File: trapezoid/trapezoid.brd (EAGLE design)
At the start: 59.7 x 28.6 mm, 33 parts, among them U1 MMA8452Q, U4 MCP73831, Y1 CRYSTAL.ABS25

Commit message: silk
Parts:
- C6: value 0.1uF -> 1.0uF
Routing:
- net N$9: track 5.24 -> 5.87 mm
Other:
- board text added: "0.1uF"
- board text added: "1.0uF"
- board text added: "10"
- board text added: "10k"
- board text added: "11"
- board text added: "12"
- board text added: "13"
- board text added: "2"
- board text added: "2k"
- board text added: "330"
- board text added: "4.7uF"
- board text added: "47k"
- board text added: "ABS25"
- board text added: "CR1225"
- board text added: "DS1339"
- board text added: "FXAS21002"
- board text added: "GND"
- board text added: "MCP73831"
- board text added: "MMA8452Q"
- board text added: "Micron uSD"
- board text added: "RAW"
- board text added: "Sharkduino V2"
- board text added: "VCC"
- board text added: "VIMS"
- board text added: "W&M Physics"
- board text added: "W&M Physics VIMS"
- board text added: "William Laney"
- board text added: "William Laney 2016"
- board text added: "X"
- board text added: "Y"
- board text added: "Z"
- board text added: "uUSB"
- board text added: "welaney@email.wm.edu"
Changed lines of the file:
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@@
 <wire x1="22.225" y1="1.27" x2="22.225" y2="19.05" width="0.3048" layer="21"/>
 <circle x="36.4236" y="11.811" radius="0.289603125" width="0.254" layer="21"/>
+<wire x1="23.876" y1="20.193" x2="24.892" y2="20.193" width="0.254" layer="21"/>
+<wire x1="23.876" y1="20.193" x2="24.257" y2="19.812" width="0.254" layer="21"/>
+<wire x1="23.876" y1="20.193" x2="24.257" y2="20.574" width="0.254" layer="21"/>
+<wire x1="26.289" y1="20.701" x2="26.289" y2="19.685" width="0.254" layer="21"/>
+<wire x1="26.289" y1="20.701" x2="25.908" y2="20.32" width="0.254" layer="21"/>
+<wire x1="26.289" y1="20.701" x2="26.67" y2="20.32" width="0.254" layer="21"/>
+<circle x="22.733" y="20.193" radius="0.127" width="0.254" layer="21"/>
+<text x="25.781" y="21.717" size="1.016" layer="21" font="vector" ratio="15" rot="R270">X</text>
+<text x="24.003" y="21.717" size="1.016" layer="21" font="vector" ratio="15" rot="R270">Y</text>
+<text x="22.225" y="21.717" size="1.016" layer="21" font="vector" ratio="15" rot="R270">Z</text>
+<text x="8.509" y="15.24" size="1.016" layer="21" font="vector" ratio="15">Sharkduino V2</text>
+<text x="35.56" y="24.892" size="0.8128" layer="21" font="vector" ratio="15" rot="R90">0.1uF</text>
+<text x="37.592" y="21.844" size="0.8128" layer="21" font="vector" ratio="15" rot="R90">10k</text>
+<text x="41.402" y="21.844" size="0.8128" layer="21" font="vector" ratio="15" rot="R90">330</text>
+<text x="45.466" y="22.098" size="0.8128" layer="21" font="vector" ratio="15">4.7uF</text>
+<text x="51.054" y="26.924" size="0.8128" layer="21" font="vector" ratio="15">2k</text>
+<text x="50.546" y="19.558" size="0.8128" layer="21" font="vector" ratio="15" rot="R90">4.7uF</text>
+<text x="44.704" y="15.494" size="0.8128" layer="21" font="vector" ratio="15">0.1uF</text>
+<text x="50.8" y="10.0965" size="0.8128" layer="21" font="vector" ratio="15" rot="R90">0.1uF</text>
+<text x="30.2514" y="11.2014" size="0.8128" layer="21" font="vector" ratio="15" rot="R90">0.1uF</text>
+<text x="27.686" y="11.176" size="0.8128" layer="21" font="vector" ratio="15" rot="R90">1.0uF</text>
+<text x="32.1056" y="9.6774" size="0.8128" layer="21" font="vector" ratio="15">0.1uF</text>
+<text x="28.321" y="9.7028" size="0.8128" layer="21" font="vector" ratio="15">0.1uF</text>
+<text x="38.608" y="4.572" size="0.8128" layer="21" font="vector" ratio="15" rot="R90">10k</text>
+<text x="44.958" y="4.572" size="0.8128" layer="21" font="vector" ratio="15" rot="R90">10k</text>
+<text x="39.624" y="9.144" size="0.8128" layer="21" font="vector" ratio="15" rot="R90">10k</text>
+<text x="35.306" y="5.588" size="0.8128" layer="21" font="vector" ratio="15">47k</text>
+<text x="46.2915" y="10.0965" size="0.8128" layer="21" font="vector" ratio="15" rot="R90">4.7uF</text>
+<text x="22.352" y="27.178" size="0.8128" layer="21" font="vector" ratio="15">ABS25</text>
+<text x="29.972" y="25.146" size="0.8128" layer="21" font="vector" ratio="15">DS1339</text>
+<text x="33.528" y="15.24" size="0.8128" layer="21" font="vector" ratio="15">FXAS21002</text>
+<text x="41.275" y="8.8265" size="0.8128" layer="21" font="vector" ratio="15">MMA8452Q</text>
+<text x="40.4495" y="25.146" size="0.8128" layer="21" font="vector" ratio="15">MCP73831</text>
+<text x="9.652" y="2.286" size="0.8128" layer="21" font="vector" ratio="15">CR1225</text>
+<text x="59.436" y="11.049" size="0.8128" layer="21" font="vector" ratio="15" rot="R90">RAW</text>
+<text x="59.436" y="8.382" size="0.8128" layer="21" font="vector" ratio="15" rot="R90">GND</text>
+<text x="47.879" y="0.254" size="0.8128" layer="21" font="vector" ratio="15">GND</text>
+<text x="50.673" y="0.254" size="0.8128" layer="21" font="vector" ratio="15">RAW</text>
+<text x="42.799" y="0.254" size="0.8128" layer="21" font="vector" ratio="15">VCC</text>
+<text x="22.733" y="0.254" size="0.8128" layer="21" font="vector" ratio="15">10</text>
+<text x="25.4" y="0.254" size="0.8128" layer="21" font="vector" ratio="15">11</text>
+<text x="27.94" y="0.254" size="0.8128" layer="21" font="vector" ratio="15">12</text>
+<text x="30.48" y="0.254" size="0.8128" layer="21" font="vector" ratio="15">13</text>
+<text x="41.021" y="19.304" size="0.8128" layer="21" font="vector" ratio="15">2</text>
+<text x="42.799" y="19.304" size="0.8128" layer="21" font="vector" ratio="15">GND</text>
+<text x="10.287" y="17.145" size="1.016" layer="21" font="vector" ratio="15">William Laney</text>
+<text x="11.938" y="19.05" size="1.016" layer="21" font="vector" ratio="15">W&amp;M Physics</text>
+<text x="15.24" y="21.844" size="1.016" layer="21" font="vector" ratio="15">VIMS</text>
+<text x="20.574" y="18.542" size="1.016" layer="22" font="vector" ratio="15" rot="MR0">Micron uSD</text>
+<text x="24.003" y="0.254" size="0.8128" layer="22" font="vector" ratio="15" rot="MR0">10</text>
+<text x="26.67" y="0.254" size="0.8128" layer="22" font="vector" ratio="15" rot="MR0">11</text>
+<text x="29.21" y="0.254" size="0.8128" layer="22" font="vector" ratio="15" rot="MR0">12</text>
+<text x="31.75" y="0.254" size="0.8128" layer="22" font="vector" ratio="15" rot="MR0">13</text>
+<text x="42.799" y="0.254" size="0.8128" layer="21" font="vector" ratio="15">VCC</text>
+<text x="44.831" y="0.254" size="0.8128" layer="22" font="vector" ratio="15" rot="MR0">VCC</text>
+<text x="49.911" y="0.254" size="0.8128" layer="22" font="vector" ratio="15" rot="MR0">GND</text>
+<text x="52.705" y="0.254" size="0.8128" layer="22" font="vector" ratio="15" rot="MR0">RAW</text>
+<text x="58.674" y="8.382" size="0.8128" layer="22" font="vector" ratio="15" rot="MR90">GND</text>
+<text x="59.436" y="11.049" size="0.8128" layer="21" font="vector" ratio="15" rot="R90">RAW</text>
+<text x="58.674" y="11.049" size="0.8128" layer="22" font="vector" ratio="15" rot="MR90">RAW</text>
+<text x="41.529" y="19.05" size="0.8128" layer="22" font="vector" ratio="15" rot="MR0">2</text>
+<text x="44.831" y="19.05" size="0.8128" layer="22" font="vector" ratio="15" rot="MR0">GND</text>
+<text x="45.72" y="26.67" size="1.016" layer="22" font="vector" ratio="15" rot="MR0">Sharkduino V2</text>
+<text x="45.72" y="24.638" size="1.016" layer="22" font="vector" ratio="15" rot="MR0">William Laney  2016</text>
+<text x="45.72" y="22.606" size="1.016" layer="22" font="vector" ratio="15" rot="MR0">W&amp;M Physics  VIMS</text>
+<text x="45.72" y="20.828" size="1.016" layer="22" font="vector" ratio="15" rot="MR0">welaney@email.wm.edu</text>
+<text x="58.928" y="22.352" size="0.8128" layer="21" font="vector" ratio="15" rot="R90">uUSB</text>
+<wire x1="2.54" y1="1.397" x2="3.556" y2="1.397" width="0.254" layer="21"/>
+<wire x1="2.54" y1="1.397" x2="2.921" y2="1.016" width="0.254" layer="21"/>
+<wire x1="2.54" y1="1.397" x2="2.921" y2="1.778" width="0.254" layer="21"/>
+<wire x1="4.953" y1="1.905" x2="4.953" y2="0.889" width="0.254" layer="21"/>
+<wire x1="4.953" y1="1.905" x2="4.572" y2="1.524" width="0.254" layer="21"/>
+<wire x1="4.953" y1="1.905" x2="5.334" y2="1.524" width="0.254" layer="21"/>
+<circle x="1.397" y="1.397" radius="0.127" width="0.254" layer="21"/>
+<text x="4.445" y="2.921" size="1.016" layer="21" font="vector" ratio="15" rot="R270">X</text>
+<text x="2.667" y="2.921" size="1.016" layer="21" font="vector" ratio="15" rot="R270">Y</text>
+<text x="0.889" y="2.921" size="1.016" layer="21" font="vector" ratio="15" rot="R270">Z</text>
+<wire x1="57.785" y1="5.715" x2="58.801" y2="5.715" width="0.254" layer="21"/>
+<wire x1="57.785" y1="5.715" x2="58.166" y2="5.334" width="0.254" layer="21"/>
+<wire x1="57.785" y1="5.715" x2="58.166" y2="6.096" width="0.254" layer="21"/>
+<circle x="58.293" y="2.159" radius="0.127" width="0.254" layer="21"/>
+<text x="56.769" y="3.429" size="1.016" layer="21" font="vector" ratio="15">X</text>
+<text x="56.769" y="5.207" size="1.016" layer="21" font="vector" ratio="15">Y</text>
+<text x="56.769" y="1.651" size="1.016" layer="21" font="vector" ratio="15">Z</text>
+<wire x1="58.293" y1="4.445" x2="58.293" y2="3.429" width="0.254" layer="21"/>
+<wire x1="58.293" y1="4.445" x2="57.912" y2="4.064" width="0.254" layer="21"/>
+<wire x1="58.293" y1="4.445" x2="58.674" y2="4.064" width="0.254" layer="21"/>
 </plain>
 <attributes>
@@
 <element name="C4" library="microbuilder" package="0805-NO" value="0.1uF" x="29.845" y="8.89" rot="R180"/>
 <element name="C5" library="microbuilder" package="0805-NO" value="0.1uF" x="31.115" y="12.7" rot="R90"/>
-<element name="C6" library="microbuilder" package="0805-NO" value="0.1uF" x="28.575" y="12.7" rot="R90"/>
+<element name="C6" library="microbuilder" package="0805-NO" value="1.0uF" x="28.575" y="12.7" rot="R90"/>
 <element name="J5" library="SparkFun-Connectors" package="1X02_LOCK" value="" x="57.15" y="9.525" rot="R90"/>
 <element name="U$2" library="sharkdunio" package="MOLEX_MICROSD" value="MOLEX_MICROSD" x="15.875" y="6.35" rot="MR0"/>
@@
 <contactref element="R4" pad="1"/>
 <wire x1="37.335" y1="12.7" x2="38.1" y2="12.7" width="0.254" layer="1"/>
+<wire x1="38.1" y1="12.7" x2="38.735" y2="12.065" width="0.254" layer="1"/>
+<wire x1="38.735" y1="12.065" x2="38.735" y2="10.16" width="0.254" layer="1"/>
+<wire x1="38.735" y1="10.16" x2="38.1" y2="9.525" width="0.254" layer="1"/>
+<wire x1="38.1" y1="9.525" x2="37.15" y2="9.525" width="0.254" layer="1"/>
 <wire x1="37.15" y1="9.525" x2="36.83" y2="9.205" width="0.254" layer="1"/>
-<wire x1="38.1" y1="12.7" x2="38.1" y2="10.475" width="0.254" layer="1"/>
-<wire x1="38.1" y1="10.475" x2="36.83" y2="9.205" width="0.254" layer="1"/>
 </signal>
 <signal name="N$10">

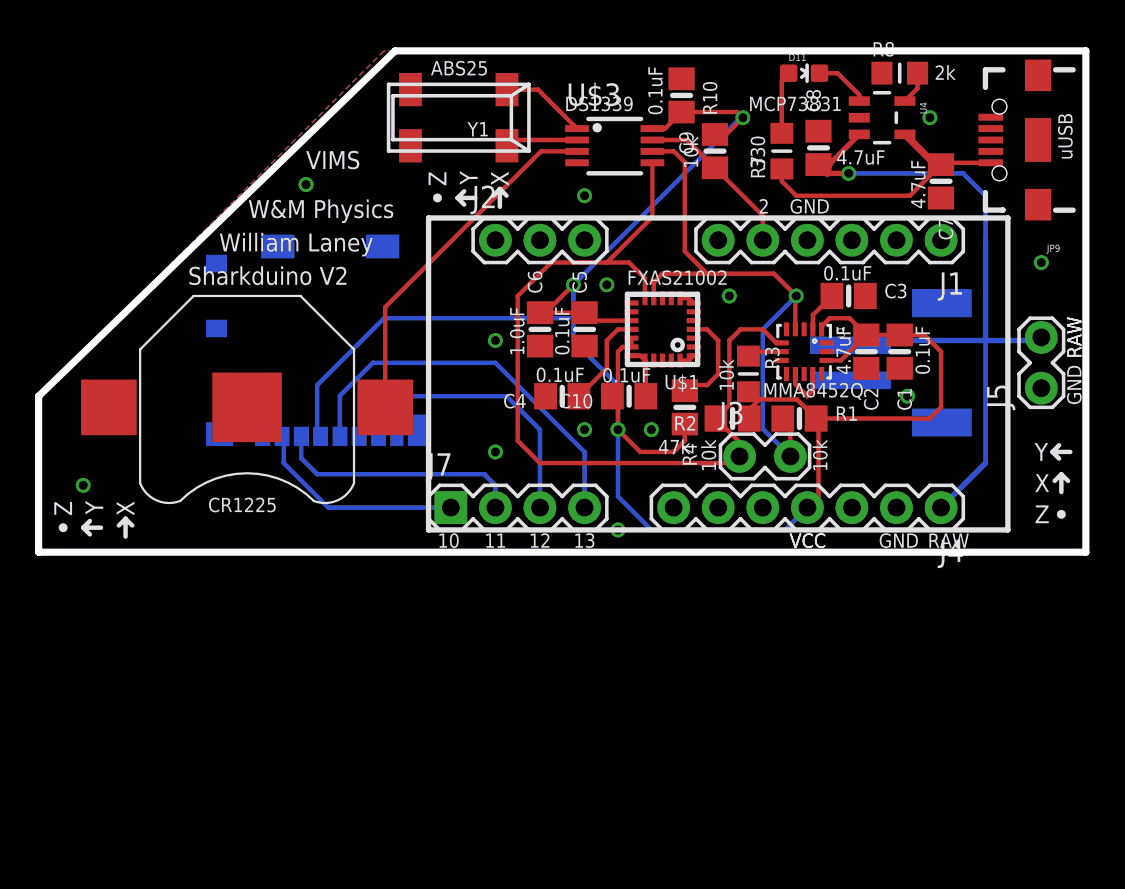
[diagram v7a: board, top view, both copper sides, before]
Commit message: shrunk board
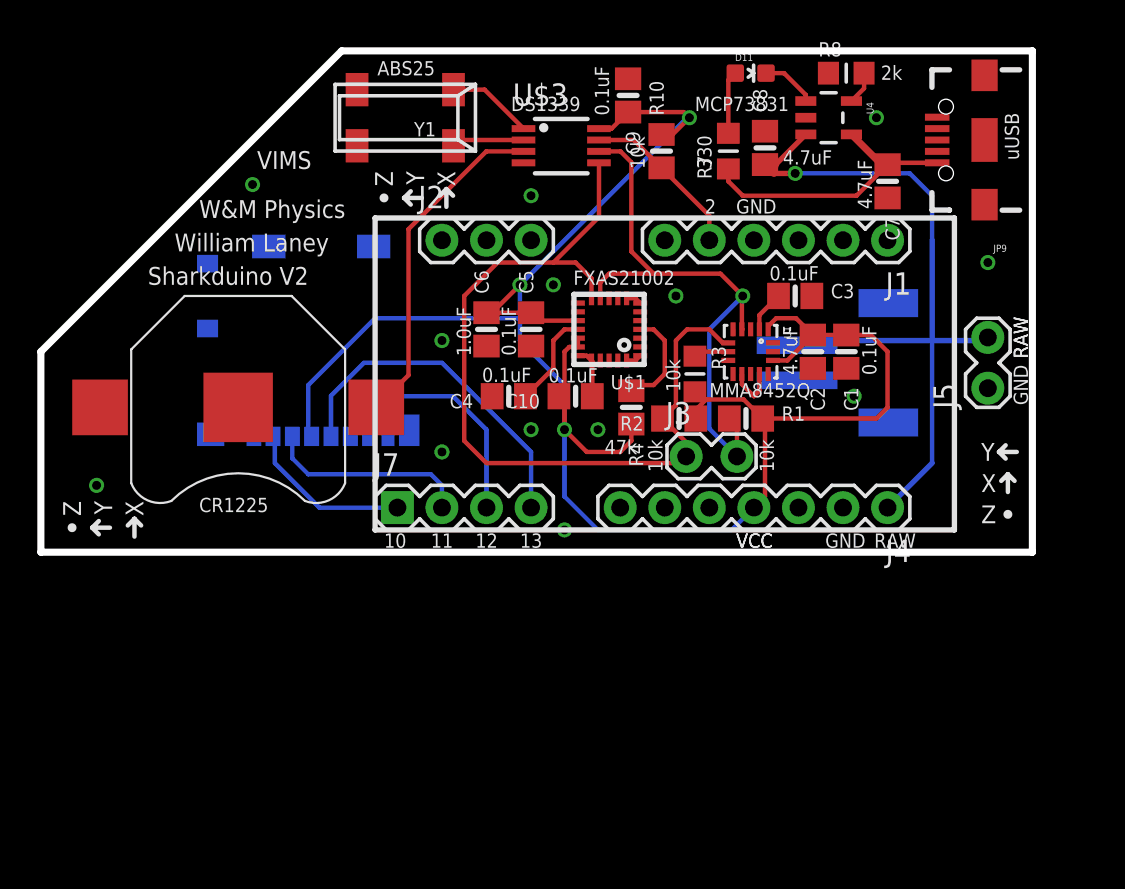
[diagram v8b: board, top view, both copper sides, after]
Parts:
- moved C1 3.05 mm to (46.0, 11.4)
- moved C10 3.05 mm to (30.6, 8.89)
- moved C3 3.05 mm to (43.1, 14.6)
- moved C7 3.05 mm to (48.4, 21.1)
- moved C8 3.05 mm to (41.4, 23.0)
- moved C9 3.05 mm to (33.6, 26.0)
- moved D11 3.05 mm to (40.6, 27.3)
- moved J1 3.05 mm to (48.4, 17.8)
- moved J2 3.05 mm to (23.0, 17.8)
- moved J4 3.05 mm to (48.4, 2.54)
- moved J5 3.05 mm to (54.1, 9.53)
- moved J7 3.05 mm to (20.4, 2.54)
- moved JP9 3.05 mm to (53.9, 23.5)
- moved R1 3.05 mm to (40.3, 7.62)
- moved R2 3.05 mm to (36.5, 7.62)
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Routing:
- net +3V3: track 118.3 -> 115.8 mm
- net SD_CS: track 12.1 -> 9.60 mm
- net MOSI: track 14.2 -> 11.7 mm
- net SCK: track 22.3 -> 19.8 mm
- net MISO: track 16.2 -> 13.6 mm
- net N$4: track 20.3 -> 19.3 mm
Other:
- board size 59.7 x 28.6 mm -> 56.5 x 28.6 mm
